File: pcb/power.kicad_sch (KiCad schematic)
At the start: 24 parts, among them J3 XT30PW-M, Q2 NTR4003N, Q4 NTR4003N, Q5 Si3407DV, U3 TPS561246DRLR

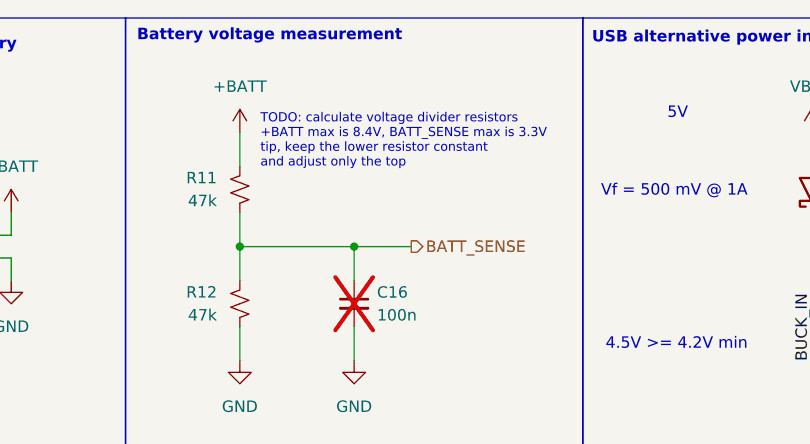
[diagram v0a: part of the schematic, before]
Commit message: Updated batt sense voltage divider
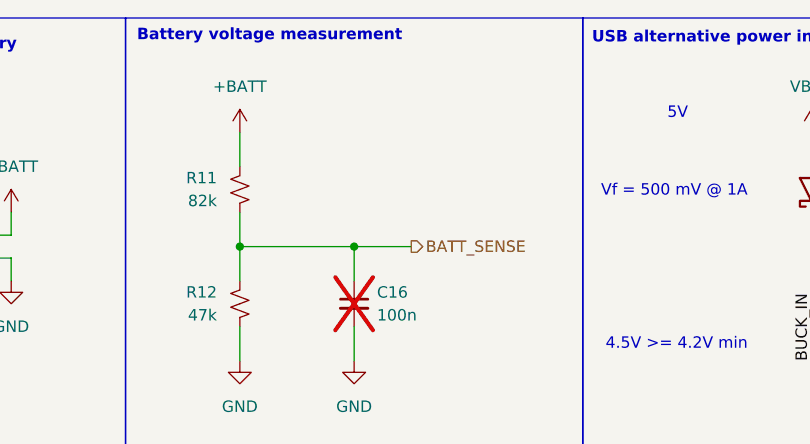
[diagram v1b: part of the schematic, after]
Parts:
- R11: value 47k -> 82k
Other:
- note removed: "TODO: calculate voltage divider resistors +BATT max is 8.4V, BATT_SENSE max is 3.3V tip, keep the lower resistor constant and adjust only the top"
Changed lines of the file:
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@@
 		)
 	)
-	(text "TODO: calculate voltage divider resistors\n+BATT max is 8.4V, BATT_SENSE max is 3.3V\ntip, keep the lower resistor constant\nand adjust only the top\n"
-		(exclude_from_sim no)
-		(at 65.786 23.368 0)
-		(effects
-			(font
-				(size 1.016 1.016)
-			)
-			(justify left top)
-		)
-	)
 	(text "Battery power switch"
 		(exclude_from_sim no)
@@
 			)
 		)
-		(property "Value" "47k"
+		(property "Value" "82k"
 			(at 60.96 33.0199 0)
 			(effects

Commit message: Start layout
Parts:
- added C22: 100n, Capacitor_SMD:C_0603_1608Metric, symbol Device:C_Small
- added R14: PA0805FRE7W0R002L, Resistor_SMD:R_0805_2012Metric, symbol Device:R_Small_US
- added SW7, SW8: SW_SPDT, symbol Switch:SW_SPDT
- added U3: ZXCT180A4W5, Package_TO_SOT_SMD:SOT-23-5, symbol DI_ZXCT180:ZXCT180A4
- C16: renamed from C17; footprint (none) -> Capacitor_SMD:C_0805_2012Metric
- C18: renamed from C19; footprint (none) -> Capacitor_SMD:C_0603_1608Metric
- C19: renamed from C16; footprint (none) -> Capacitor_SMD:C_0603_1608Metric
- C20: footprint (none) -> Capacitor_SMD:C_0603_1608Metric
- C21: renamed from C22; footprint (none) -> Capacitor_SMD:C_0805_2012Metric
- L1: value 2.2u -> AMPI0640ED2R2MT; footprint (none) -> L_Arlitech:L_Arlitech_AMPI0640ED2R2MT_6.6mm_7.1mm_2628_6671_Metric
- R10: renamed from R28; footprint (none) -> Resistor_SMD:R_0603_1608Metric
- R11: renamed from R27; footprint (none) -> Resistor_SMD:R_0603_1608Metric
- R12: renamed from R9; footprint (none) -> Resistor_SMD:R_0603_1608Metric
- R13: renamed from R10; footprint (none) -> Resistor_SMD:R_0603_1608Metric
- R3: renamed from R24; footprint (none) -> Resistor_SMD:R_0603_1608Metric
- R4: renamed from R8; footprint (none) -> Resistor_SMD:R_0603_1608Metric
- R5: renamed from R19; footprint (none) -> Resistor_SMD:R_0603_1608Metric
- R6: renamed from R26; footprint (none) -> Resistor_SMD:R_0603_1608Metric
- R9: renamed from R25; footprint (none) -> Resistor_SMD:R_0603_1608Metric
- renumbered C18 to C17, D2 to D1, J3 to J1, Q2 to Q1, Q4 to Q2, Q5 to Q3, R11 to R7, R12 to R8, U3 to U2
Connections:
- net +3V3: now also C22.1, U3.5 (VS)
- net +BATT: now also R14.2, U3.4 (IN-); no longer J1.2 (Pin_2), R7.1
- net GND: now also C22.2, SW8.3 (C), U3.2 (GND)
- net at R4.2, U2.5 (EN): now also SW8.2 (B)
- net BATT_SENSE renamed BATT_VSENSE
- new net BATT_ISENSE: U3.1 (OUT)
- new net BATT_MEAS: J1.2 (Pin_2), R14.1, R7.1, U3.3 (IN+)
- no-connect marks 0 -> 1
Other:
- note added: "2 mOhm 1% 1/4W 0805"
- note added: "2.2uH 10mOhm"
- note added: "Battery current sense"
- note added: "Cbypass"
- note added: "USB alt power in"
- note added: "Vf=500 mV at 1A"
- note added: "likely safe the resistor could burn above 11A"
- note removed: "TODO: copy paste for all other 100n caps"
- note removed: "USB alternative power in"
- note removed: "Vf = 500 mV @ 1A"
- moved on the sheet: C16, C17, C18, C19, C20, C21, D1, J1, L1, Q1, Q2, Q3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

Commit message: Layout power
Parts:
- removed SW7: SW_SPDT, symbol Switch:SW_SPDT
- added TP10, TP11, TP5, TP6, TP7, TP8, TP9: RCUCTE, TestPoint_KOASpeer:TestPoint_Chip_RCUCTE_0603, symbol Connector:TestPoint
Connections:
- net +3V3: now also TP6.1
- net BATT_ISENSE: now also TP7.1
- net BATT_VSENSE: now also TP5.1
- net BUCK_IN: now also TP11.1
- net at Q2.1 (G), R6.2, R9.2: now also TP9.1
- net at Q3.3 (G), R10.2, R11.2: now also TP10.1
- net at Q1.1 (G), R3.2, R5.1: now also TP8.1
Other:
- moved on the sheet: C22

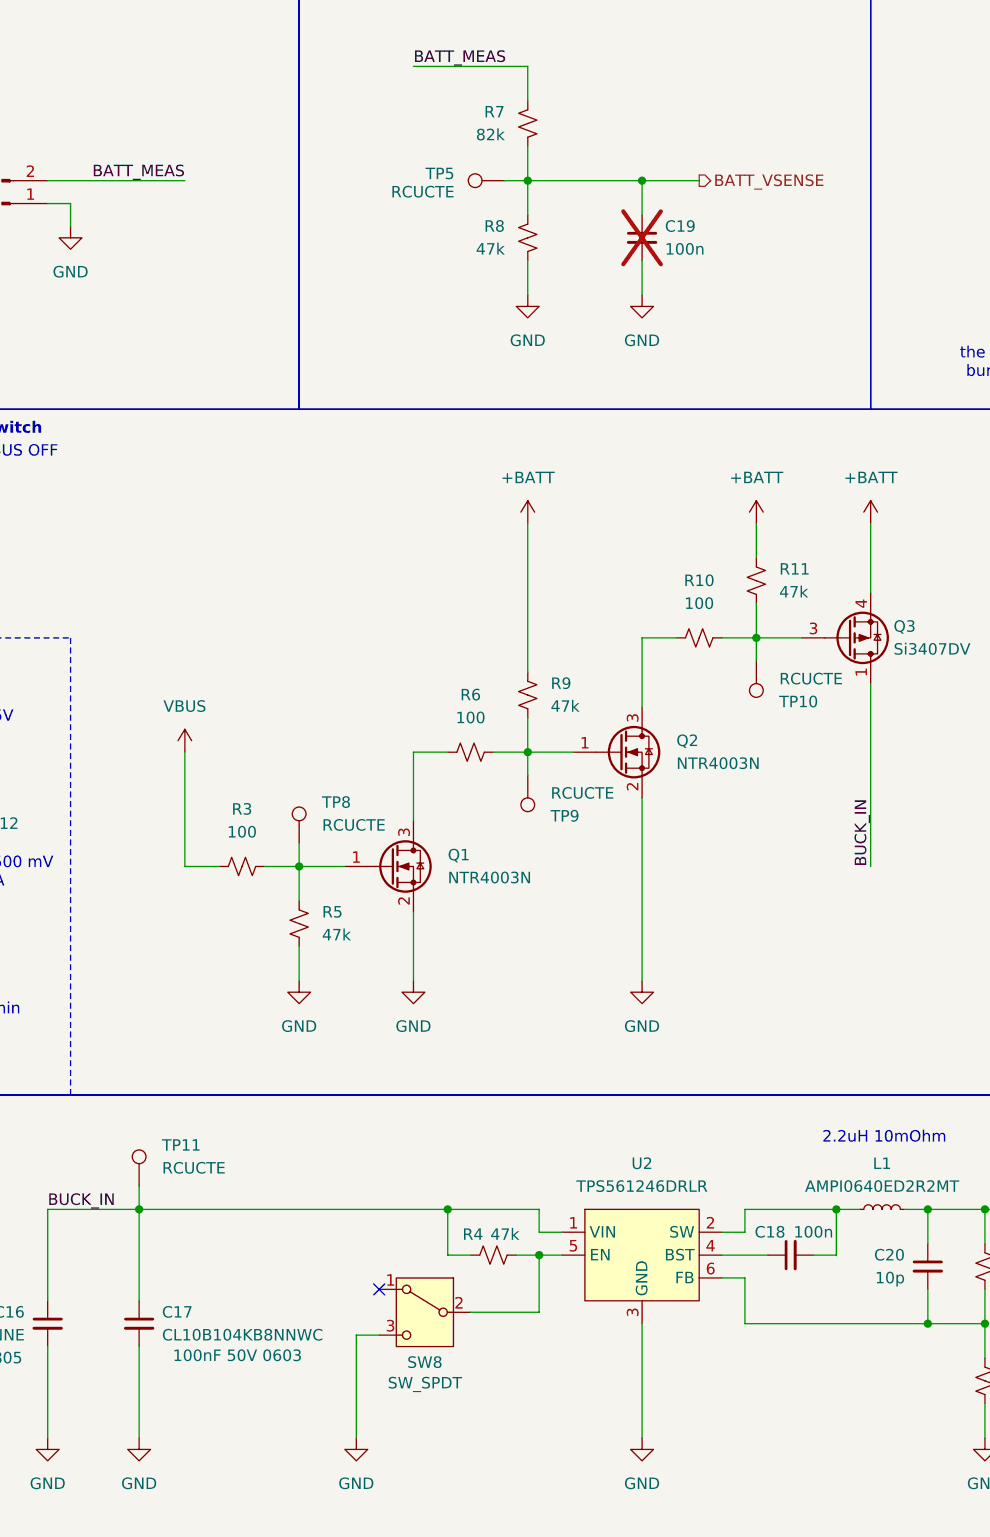
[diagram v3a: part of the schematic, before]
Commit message: Layout MCU decoupling
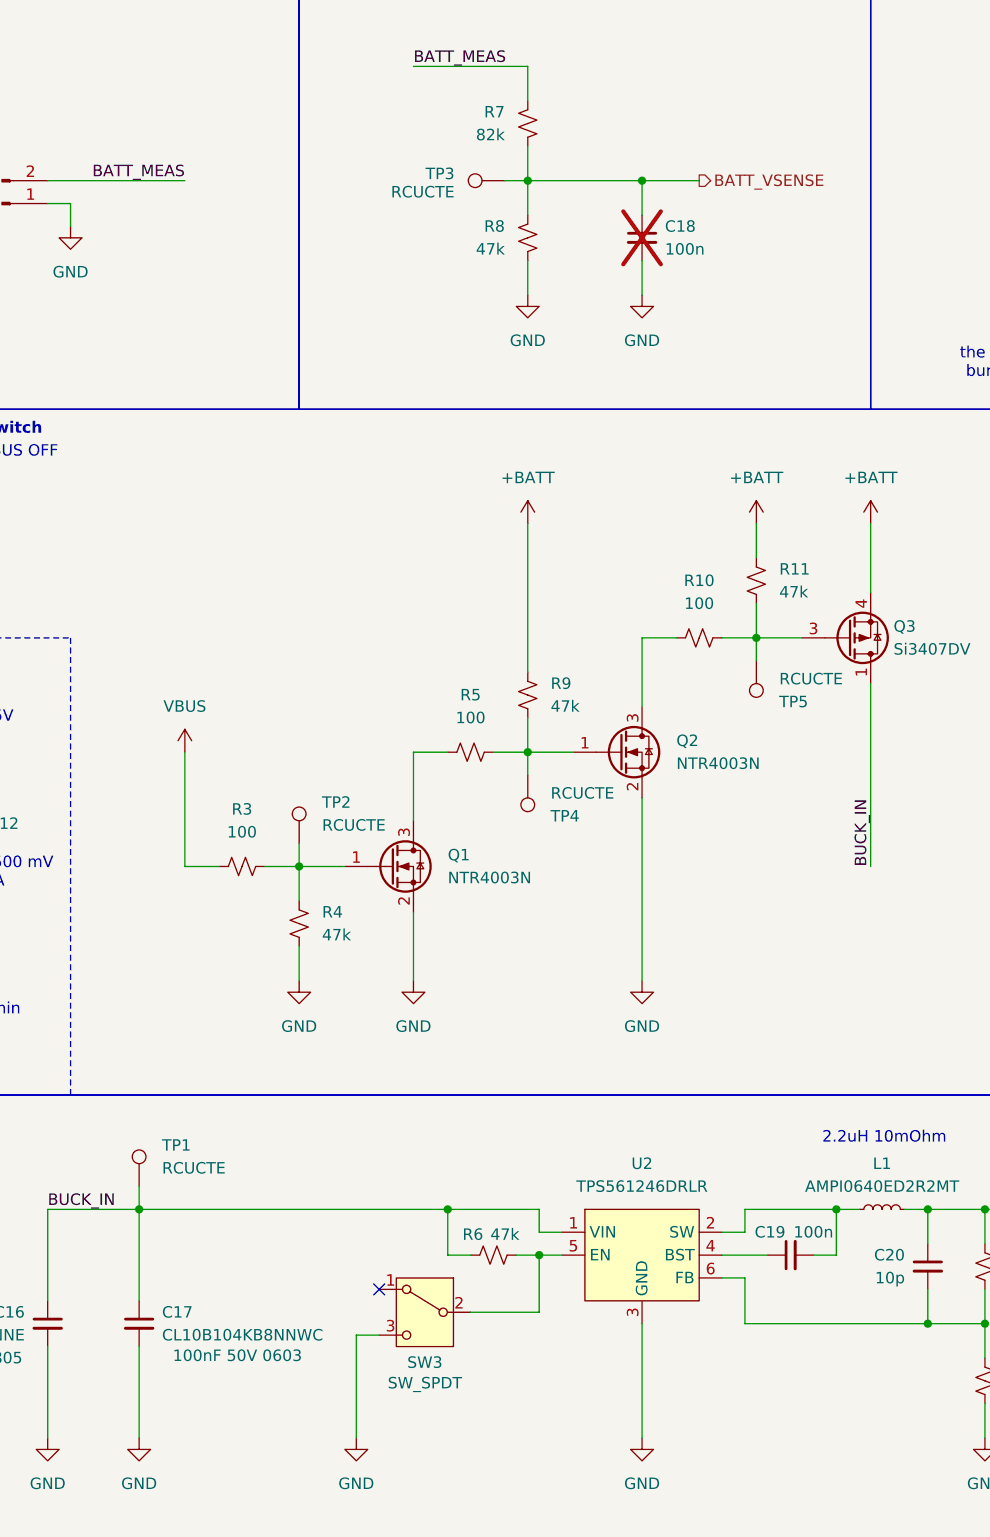
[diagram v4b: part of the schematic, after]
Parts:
- renumbered C19 to C18, C18 to C19, R5 to R4, R6 to R5, R4 to R6, SW8 to SW3, TP11 to TP1, TP8 to TP2, TP5 to TP3, TP9 to TP4, TP10 to TP5

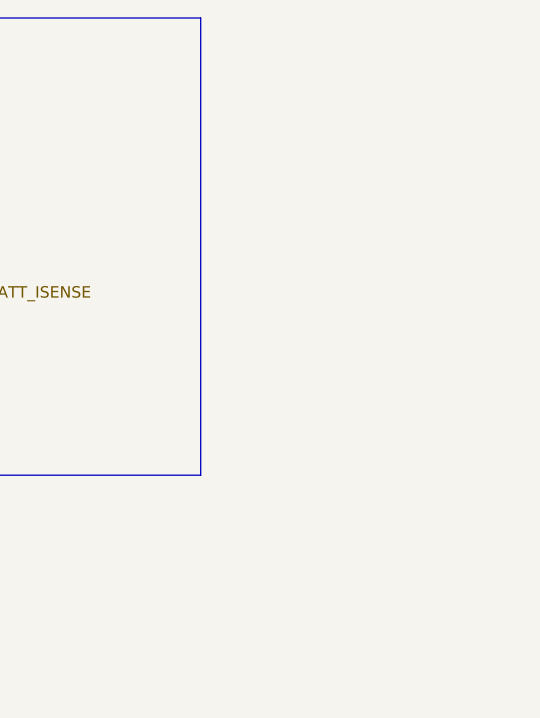
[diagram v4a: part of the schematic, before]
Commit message: Incorporate feedback servo with 4 pin molex and additional ADC channel
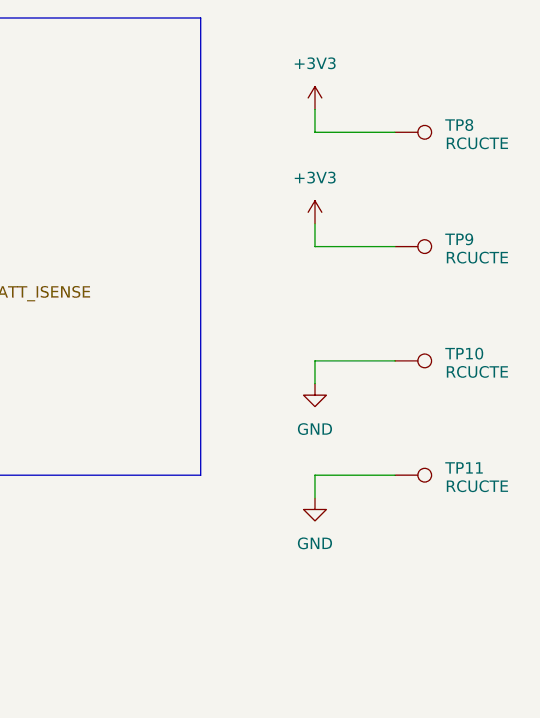
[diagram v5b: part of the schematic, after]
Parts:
- added TP10, TP11, TP8, TP9: RCUCTE, TestPoint_KOASpeer:TestPoint_Chip_RCUCTE_0603, symbol Connector:TestPoint
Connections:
- net +3V3: now also TP8.1, TP9.1
- net GND: now also TP10.1, TP11.1

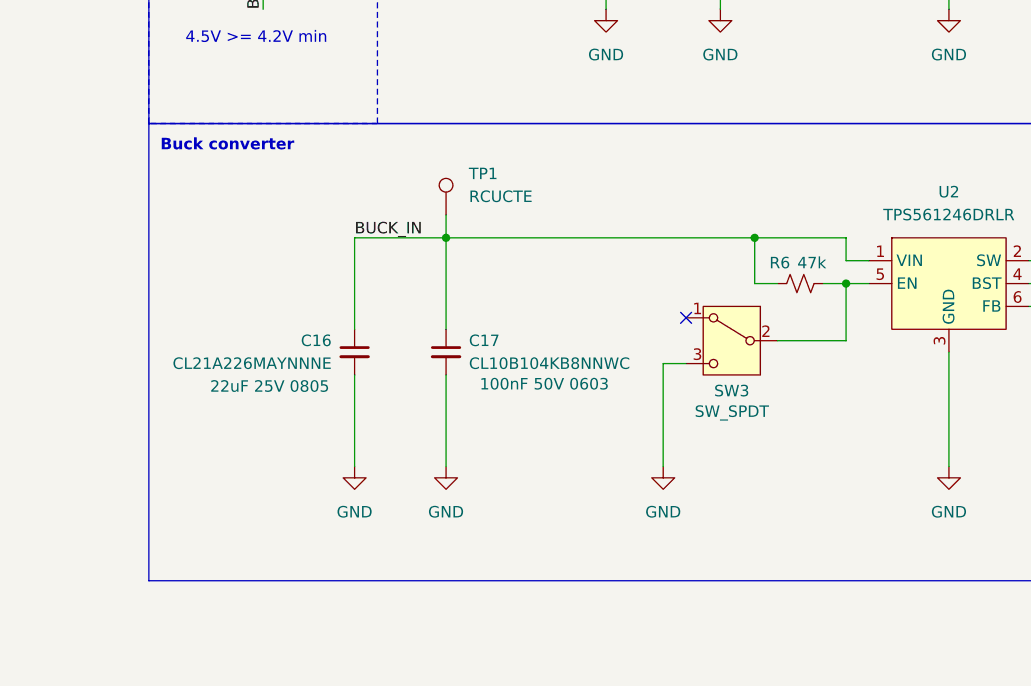
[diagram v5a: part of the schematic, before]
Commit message: Specify SPDT for buck enable
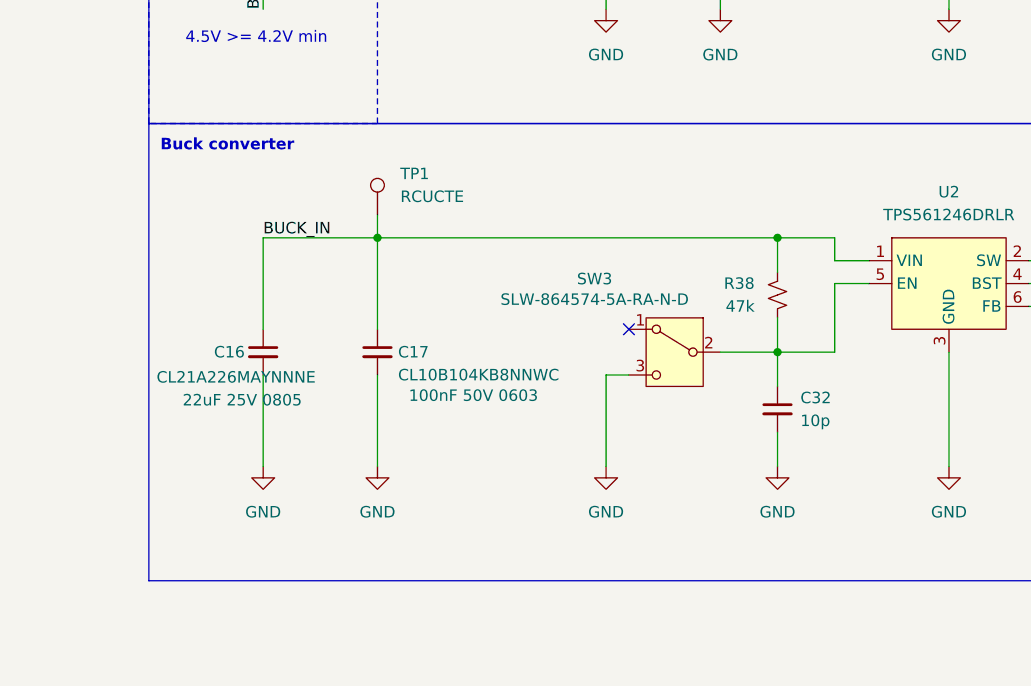
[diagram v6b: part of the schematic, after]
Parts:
- removed R6: 47k, Resistor_SMD:R_0603_1608Metric, symbol Device:R_Small_US
- added C32: 10p, Capacitor_SMD:C_0603_1608Metric, symbol Device:C_Small
- added R38: 47k, Resistor_SMD:R_0603_1608Metric, symbol Device:R_Small_US
- SW3: value SW_SPDT -> SLW-864574-5A-RA-N-D
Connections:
- net BUCK_IN: now also R38.1
- net GND: now also C32.2
- net at SW3.2 (B), U2.5 (EN): now also C32.1, R38.2
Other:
- moved on the sheet: C16, C17, SW3, TP1
